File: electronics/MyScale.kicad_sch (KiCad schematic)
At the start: 29 parts, among them J10 Conn_02x03_Odd_Even, J6 12402012E212A, J8 Conn_01x02_MountingPin, U5 STM32U083CCUx, Y1 Crystal

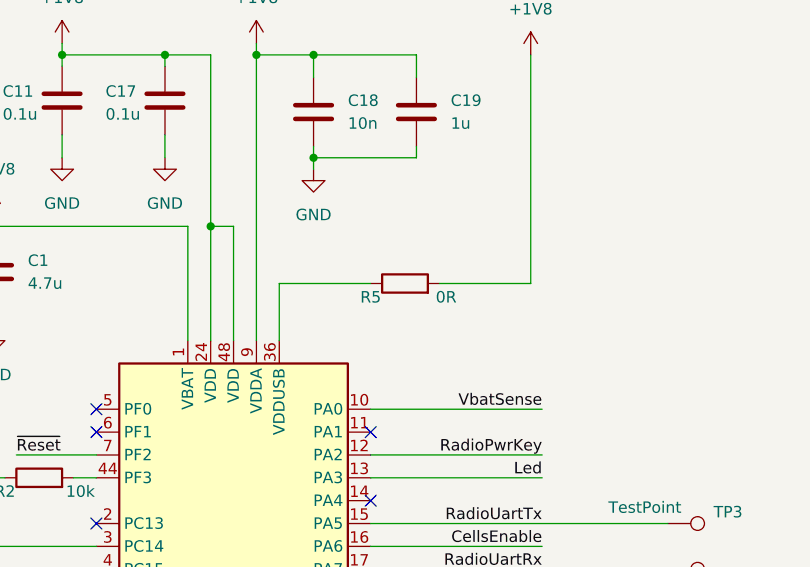
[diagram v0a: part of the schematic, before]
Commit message: electronics: add MPNs
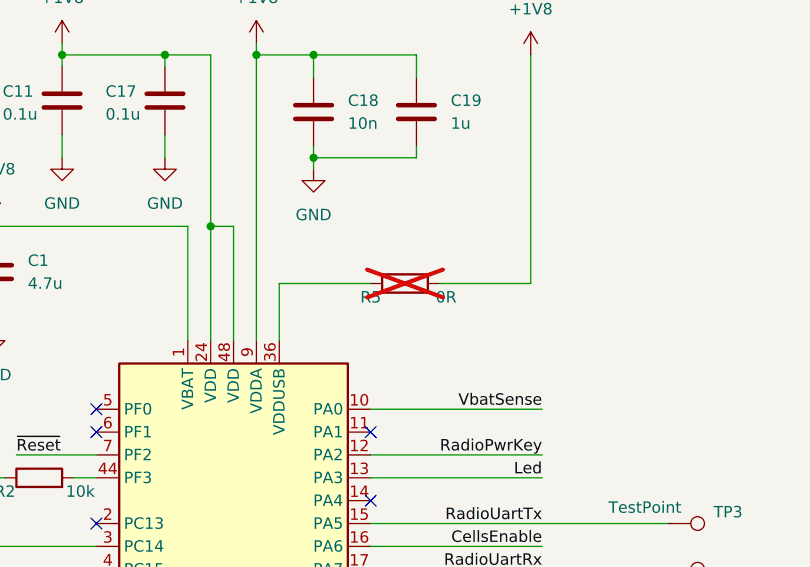
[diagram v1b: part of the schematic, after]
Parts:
- R5: now not fitted
- U5: MPN (none) -> STM32U083CCU6
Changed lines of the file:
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@@
+			)
+		)
+		(property "MPN" "STM32U083CCU6"
+			(at 212.09 104.14 0)
+			(hide yes)
+			(show_name no)
+			(do_not_autoplace no)
+			(effects
+				(font
+					(size 1.27 1.27)
+				)
 			)
 		)
@@
 		(on_board yes)
 		(in_pos_files yes)
-		(dnp no)
+		(dnp yes)
 		(property "Reference" "R5"
 			(at 227.33 61.214 90)

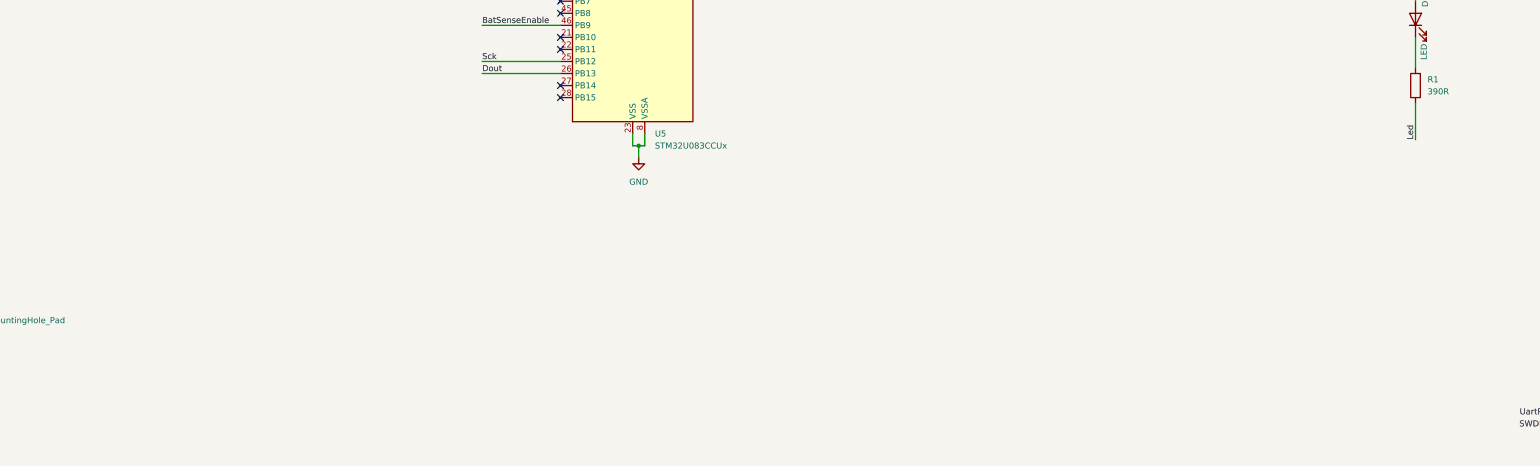
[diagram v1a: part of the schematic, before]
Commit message: electronics: simplify BOM and fix issues
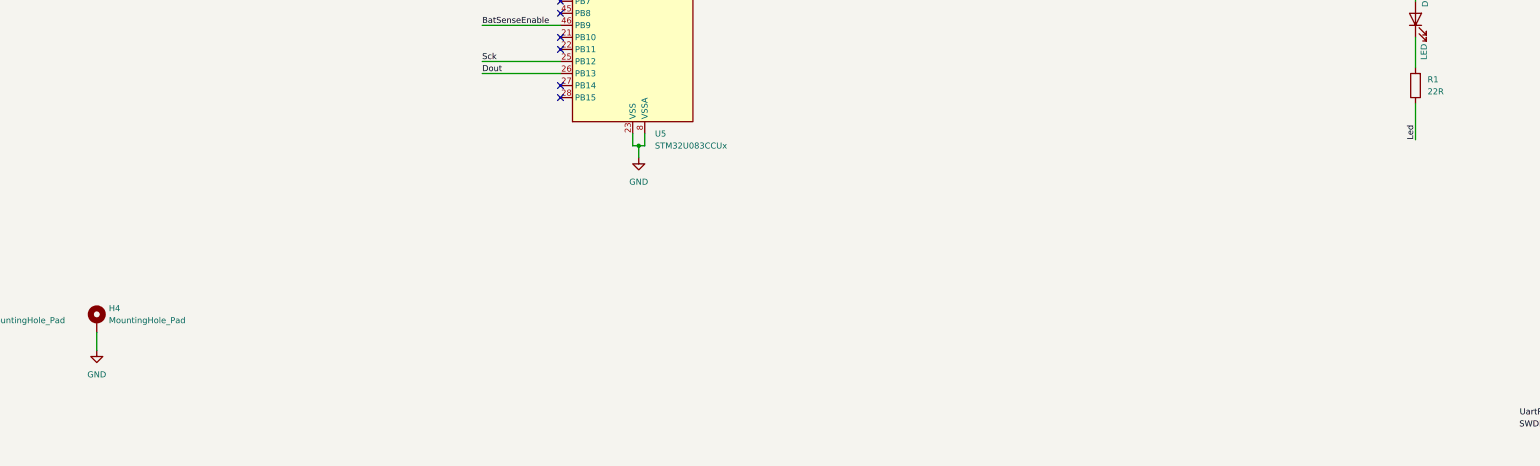
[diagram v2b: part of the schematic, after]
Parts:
- added H4: MountingHole_Pad, MountingHole:MountingHole_3.2mm_M3_Pad, symbol Mechanical:MountingHole_Pad
- R1: value 390R -> 22R
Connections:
- net GND: now also H4.1
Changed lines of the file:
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@@
 	(wire
 		(pts
+			(xy 99.06 184.15) (xy 99.06 187.96)
+		)
+		(stroke
+			(width 0)
+			(type default)
+		)
+	)
+	(wire
+		(pts
 			(xy 143.51 100.33) (xy 148.59 100.33)
 		)
@@
 			)
 		)
-		(property "Value" "390R"
+		(property "Value" "22R"
 			(at 379.73 133.3499 0)
 			(show_name no)
@@
 	)
 	(symbol
+		(lib_id "Mechanical:MountingHole_Pad")
+		(at 99.06 181.61 0)
+		(unit 1)
+		(body_style 1)
+		(exclude_from_sim no)
+		(in_bom no)
+		(on_board yes)
+		(in_pos_files yes)
+		(dnp no)
+		(fields_autoplaced yes)
+		(property "Reference" "H4"
+			(at 101.6 179.0699 0)
+			(show_name no)
+			(do_not_autoplace no)
+			(effects
+				(font
+					(size 1.27 1.27)
+				)
+				(justify left)
+			)
+		)
+		(property "Value" "MountingHole_Pad"
+			(at 101.6 181.6099 0)
+			(show_name no)
+			(do_not_autoplace no)
+			(effects
+				(font
+					(size 1.27 1.27)
+				)
+				(justify left)
+			)
+		)
+		(property "Footprint" "MountingHole:MountingHole_3.2mm_M3_Pad"
+			(at 99.06 181.61 0)
+			(hide yes)
+			(show_name no)
+			(do_not_autoplace no)
+			(effects
+				(font
+					(size 1.27 1.27)
+				)
+			)
+		)
+		(property "Datasheet" ""
+			(at 99.06 181.61 0)
+			(hide yes)
+			(show_name no)
+			(do_not_autoplace no)
+			(effects
+				(font
+					(size 1.27 1.27)
+				)
+			)
+		)
+		(property "Description" "Mounting Hole with connection"
+			(at 99.06 181.61 0)
+			(hide yes)
+			(show_name no)
+			(do_not_autoplace no)
+			(effects
+				(font
+					(size 1.27 1.27)
+				)
+			)
+		)
+		(pin "1"
+		)
+		(instances
+			(project "MyScale"
+				(path "/b5eed584-7820-40e8-871b-2aa5dd8c83ec"
+					(reference "H4")
+					(unit 1)
+				)
+			)
+		)
+	)
+	(symbol
 		(lib_id "Device:C")
 		(at 148.59 57.15 0)
@@
 					(unit 1)
 				)
+			)
+		)
+	)
+	(symbol
+		(lib_id "power:GND")
+		(at 99.06 187.96 0)
+		(unit 1)
+		(body_style 1)
+		(exclude_from_sim no)
+		(in_bom yes)
+		(on_board yes)
+		(in_pos_files yes)
+		(dnp no)
+		(fields_autoplaced yes)
+		(property "Reference" "#PWR033"
+			(at 99.06 194.31 0)
+			(hide yes)
+			(show_name no)
+			(do_not_autoplace no)
+			(effects
+				(font
+					(size 1.27 1.27)
+				)
+			)
+		)
+		(property "Value" "GND"
+			(at 99.06 193.04 0)
+			(show_name no)
+			(do_not_autoplace no)
+			(effects
+				(font
+					(size 1.27 1.27)
+				)
+			)
+		)
+		(property "Footprint" ""
+			(at 99.06 187.96 0)
+			(hide yes)
+			(show_name no)
+			(do_not_autoplace no)
+			(effects
+				(font
+					(size 1.27 1.27)
+				)
+			)
+		)
+		(property "Datasheet" ""
+			(at 99.06 187.96 0)
+			(hide yes)
+			(show_name no)
+			(do_not_autoplace no)
+			(effects
+				(font
+					(size 1.27 1.27)
+				)
+			)
+		)
+		(property "Description" "Power symbol creates a global label with name \"GND\" , ground"
+			(at 99.06 187.96 0)
+			(hide yes)
+			(show_name no)
+			(do_not_autoplace no)
+			(effects
+				(font
+					(size 1.27 1.27)
+				)
+			)
+		)
+		(pin "1"
+		)
+		(instances
+			(project "MyScale"
+				(path "/b5eed584-7820-40e8-871b-2aa5dd8c83ec"
+					(reference "#PWR033")
+					(unit 1)
+				)

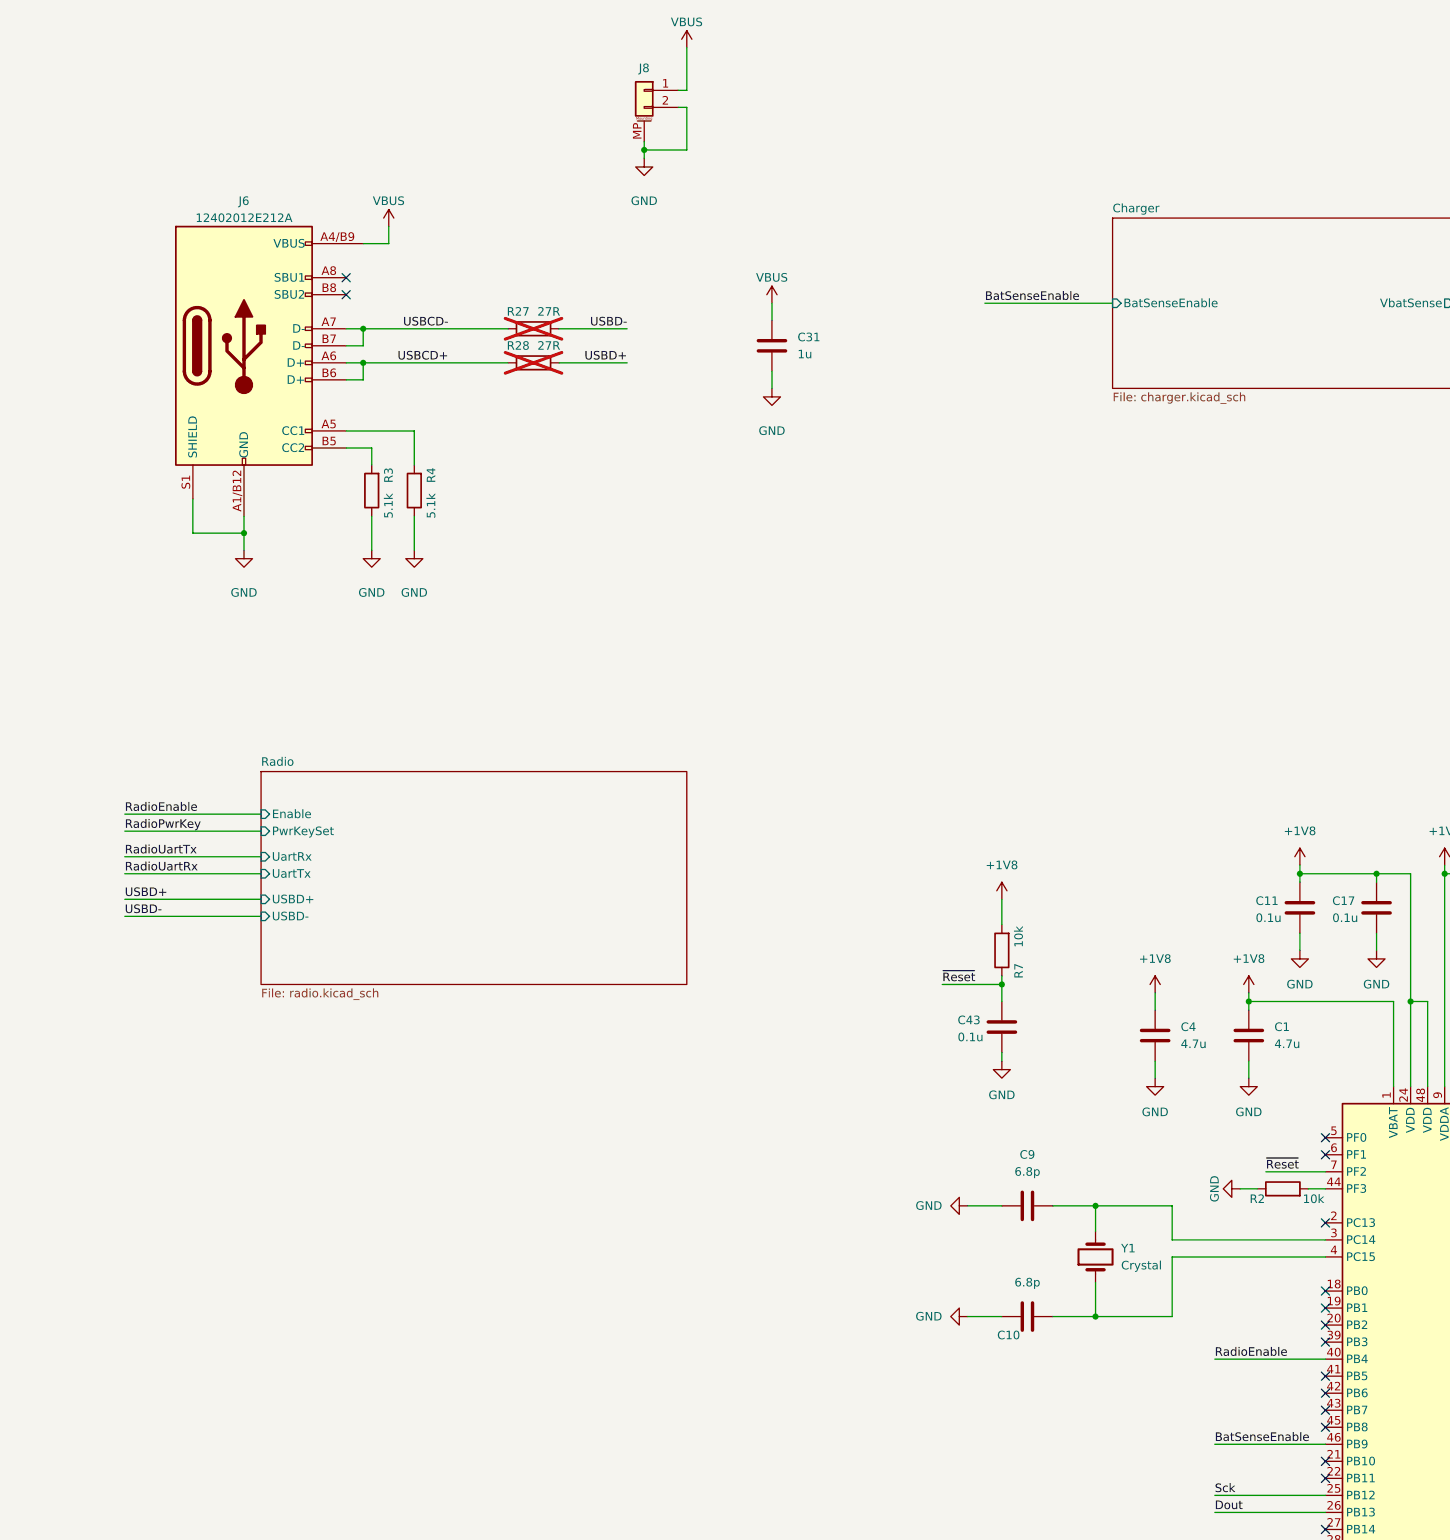
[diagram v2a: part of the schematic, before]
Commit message: electronics: improve deistribution
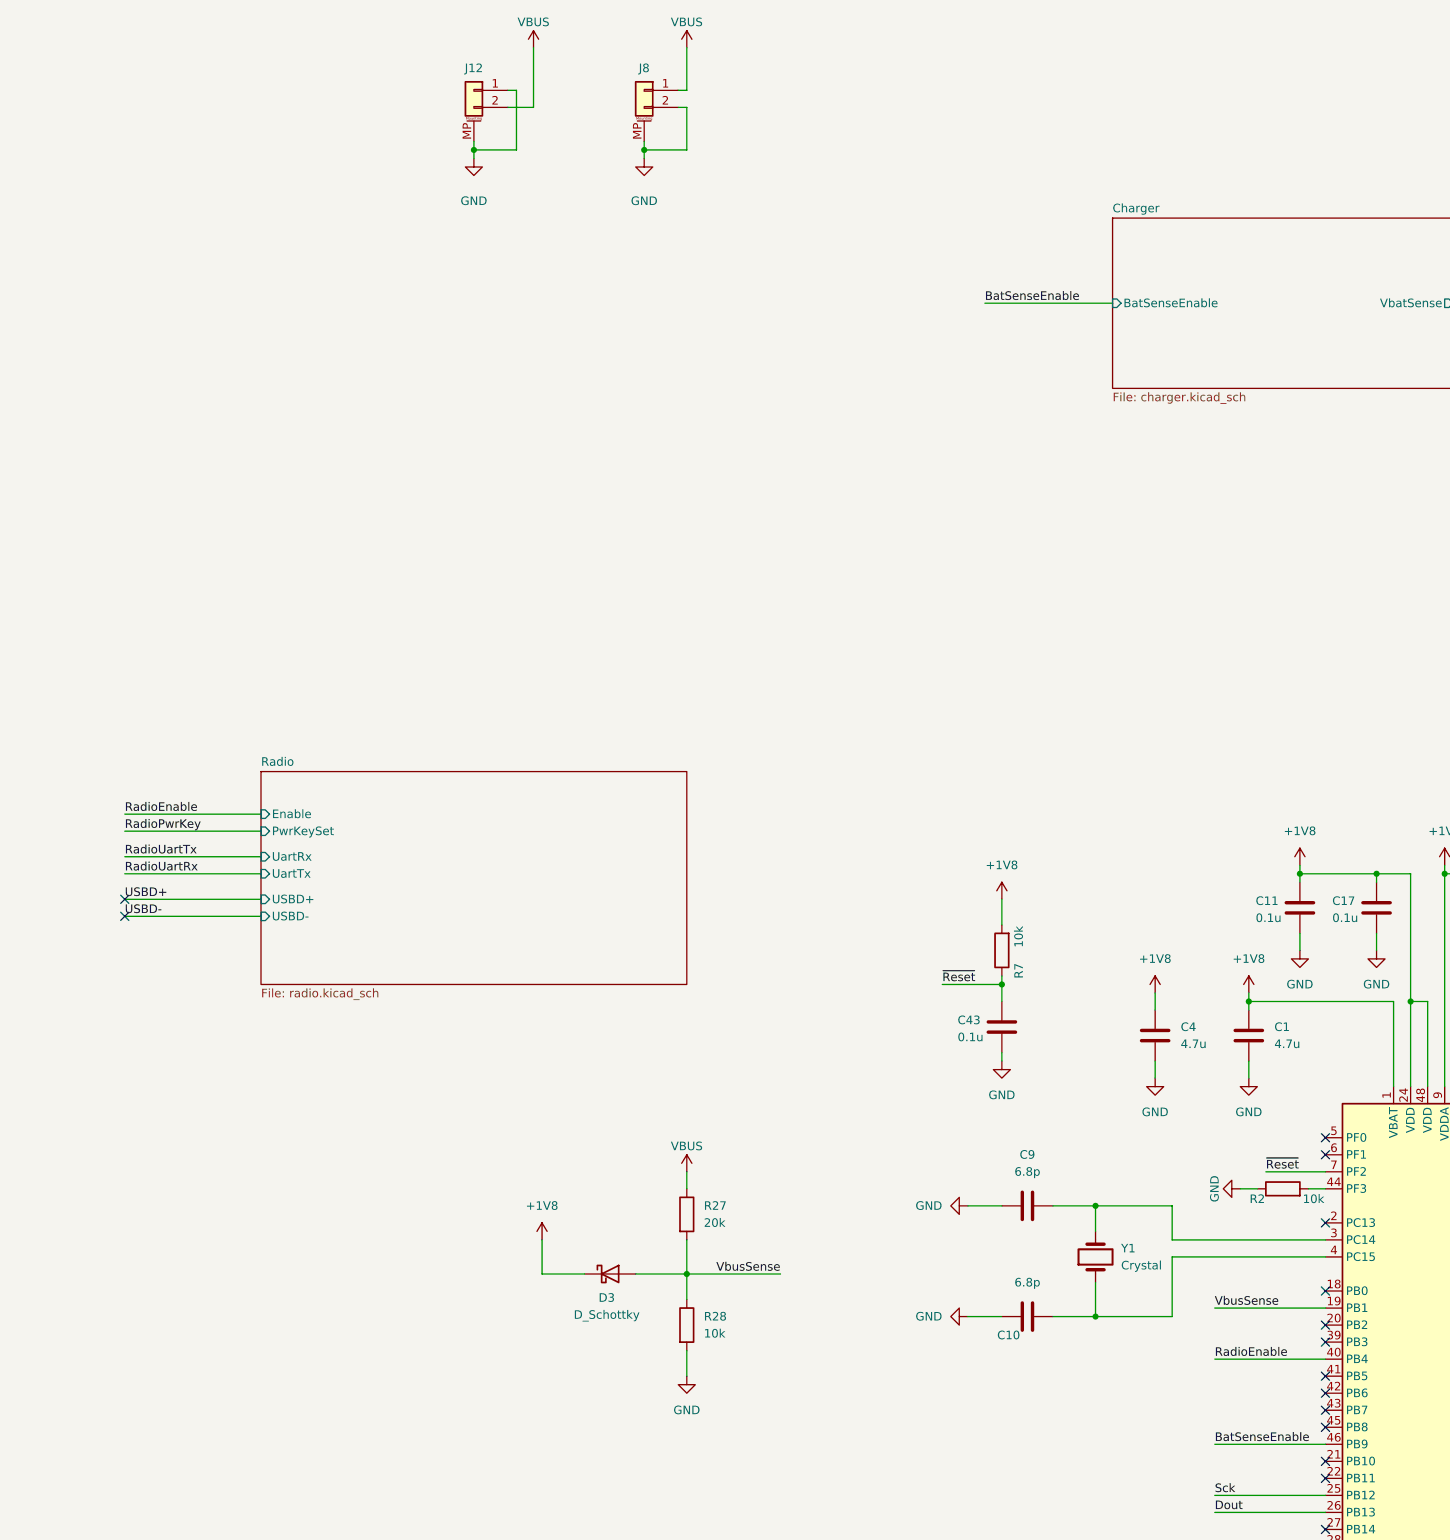
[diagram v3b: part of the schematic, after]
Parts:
- removed C31: 1u, Capacitor_SMD:C_0603_1608Metric, symbol Device:C
- removed J6: 12402012E212A, MyScale:AMPH_12402012E212A, symbol MyScale:12402012E212A
- removed R3, R4: 5.1k, Resistor_SMD:R_0603_1608Metric, symbol Device:R
- added D3: D_Schottky, Diode_SMD:D_SOD-523, symbol Device:D_Schottky
- added J12: Conn_01x02_MountingPin, MyScale:JST_S2B-PH-SM4-TB(LF)(SN), symbol Connector_Generic_MountingPin:Conn_01x02_MountingPin
- R27: value 27R -> 20k; now fitted; now in the parts list
- R28: value 27R -> 10k; now fitted; now in the parts list
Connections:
- net USBCD+ is gone; now on net GND: R28.2
- net USBCD- is gone; now on net VbusSense: R27.2
- net +1V8: now also D3.1 (K)
- net GND: now also J12.1 (Pin_1), J12.MP (MountPin)
- net USBD+: no longer R28.1
- net USBD-: no longer R27.1
- net VBUS: now also R27.1, J12.2 (Pin_2)
- net VbusSense: now reaches U5.19 (PB1)
- net VbusSense: now also R28.1, D3.2 (A)
- no-connect marks 23 -> 22

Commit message: electronics: remove testpoints from BOM
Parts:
- TP3, TP4: now left out of the parts list
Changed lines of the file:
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@@
 		(body_style 1)
 		(exclude_from_sim no)
-		(in_bom yes)
+		(in_bom no)
 		(on_board yes)
 		(in_pos_files yes)
@@
 		(body_style 1)
 		(exclude_from_sim no)
-		(in_bom yes)
-		(on_board yes)
-		(in_pos_files yes)
+		(in_bom no)
+		(on_board yes)
+		(in_pos_files yes)
